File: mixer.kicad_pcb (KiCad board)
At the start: 2 copper layers, 85.4 x 119.4 mm, 35 parts, among them J1 in1, J10 PowDistr, J11 12v, J2 in2, J3 in3, J4 power, J5 interface1, J6 interface2, J7 interface3, J8 PowDistr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

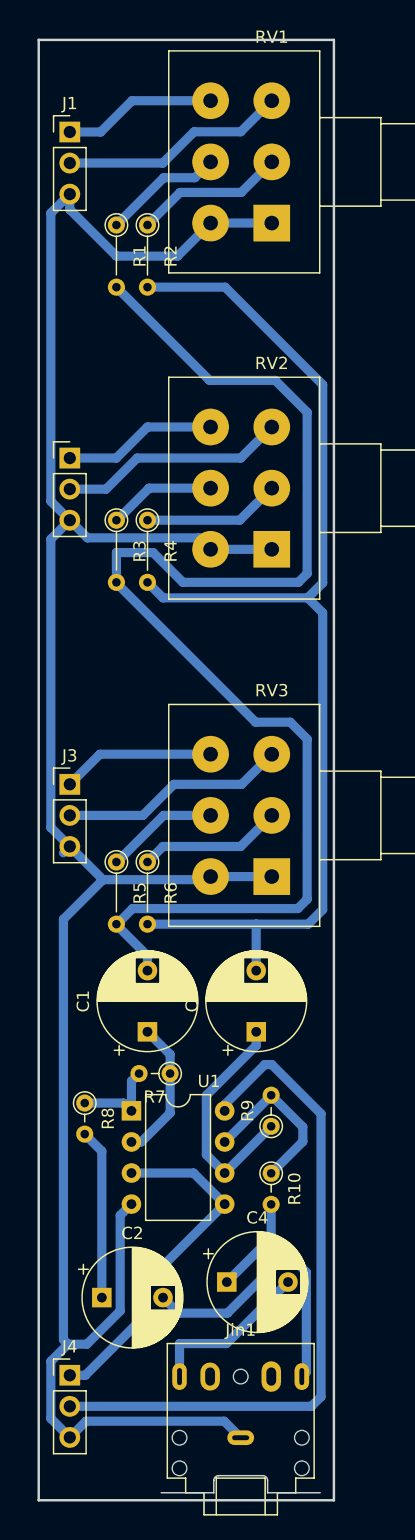
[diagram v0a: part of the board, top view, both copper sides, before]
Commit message: start creating box
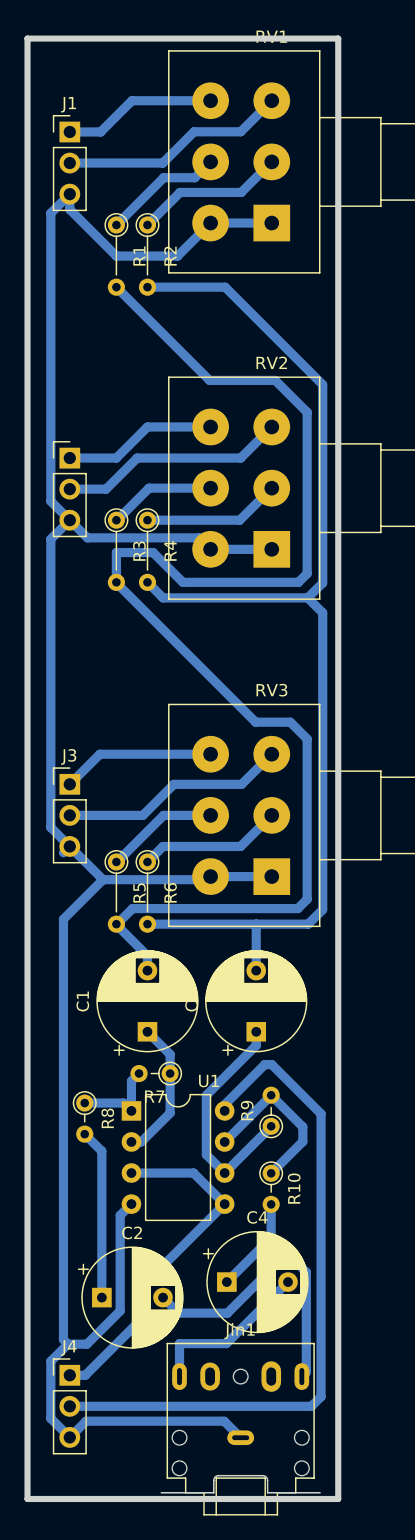
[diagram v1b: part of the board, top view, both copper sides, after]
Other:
- board size 85.4 x 119.4 mm -> 86.4 x 119.4 mm
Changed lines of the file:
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@@
   (gr_rect (start 105.46 46.25) (end 116.89 128.8)
     (stroke (width 0.5) (type default)) (fill none) (layer "Edge.Cuts"))
-  (gr_rect (start 31.445953 27.305) (end 55.575953 146.685)
-    (stroke (width 0.2) (type default)) (fill none) (layer "Edge.Cuts"))
+  (gr_rect (start 30.53 27.2) (end 55.93 146.58)
+    (stroke (width 0.5) (type default)) (fill none) (layer "Edge.Cuts"))
   (gr_circle (center 109.27 107.21) (end 110.54 107.21)
     (stroke (width 0.5) (type default)) (fill none) (layer "Edge.Cuts"))

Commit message: add box
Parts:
- moved J6 28.3 mm to (110.7, 100.9)
- moved J7 28.3 mm to (110.7, 71.7)
- moved Jin2 28.3 mm to (113.2, 54.6)
- moved J5 28.3 mm to (110.7, 130.1)
- moved C5 16.9 mm to (94.1, 93.2)
- moved C6 16.9 mm to (91.7, 122.5)
- moved J10 16.9 mm to (91.6, 71.7)
- moved J11 16.9 mm to (92.8, 53.1)
- moved J9 16.9 mm to (91.6, 100.9)
- moved R11 16.9 mm to (95.4, 60.2)
- moved R12 16.9 mm to (90.3, 67.8)
- moved J8 16.9 mm to (91.6, 130.1)
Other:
- board size 86.4 x 119.4 mm -> 90.3 x 119.4 mm

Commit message: update box
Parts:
- moved J5 28.5 mm to (85.1, 117.4)
- moved J6 28.5 mm to (85.1, 88.2)
- moved J7 28.5 mm to (85.1, 59.0)
- moved Jin2 28.5 mm to (87.6, 41.9)
- moved C5 20.8 mm to (110.5, 80.5)
- moved C6 20.8 mm to (108.1, 109.8)
- moved J10 20.8 mm to (108.0, 59.0)
- moved J9 20.8 mm to (108.0, 88.2)
- moved R12 20.8 mm to (106.7, 55.1)
- moved J11 20.8 mm to (109.2, 40.4)
- moved R11 20.8 mm to (111.8, 47.5)
- moved J8 20.8 mm to (108.0, 117.4)
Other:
- board size 90.3 x 119.4 mm -> 86.4 x 119.4 mm
